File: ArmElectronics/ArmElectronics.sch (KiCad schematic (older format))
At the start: 66 parts, among them J1 Raspberry_Pi_2_3, J2 Power In, Q1 BSS138, Q10 BSS138, Q11 BSS138, Q12 BSS138, Q13 BSS138, Q14 BSS138, Q15 BSS138, Q16 BSS138, Q17 BSS138, Q18 BSS138, Q2 BSS138, Q3 BSS138, Q4 BSS138, Q5 BSS138, Q6 BSS138, Q7 BSS138, Q8 BSS138, Q9 BSS138, U1 Teensy4.1, U10 PA-09, U2 Pololu_2857, U3 Pololu_2851, U4 BNO055_Adafruit_Breakout, U5 TB9051FTG, U6 TB9051FTG, U7 TB9051FTG, U8 PA-09, U9 PA-09

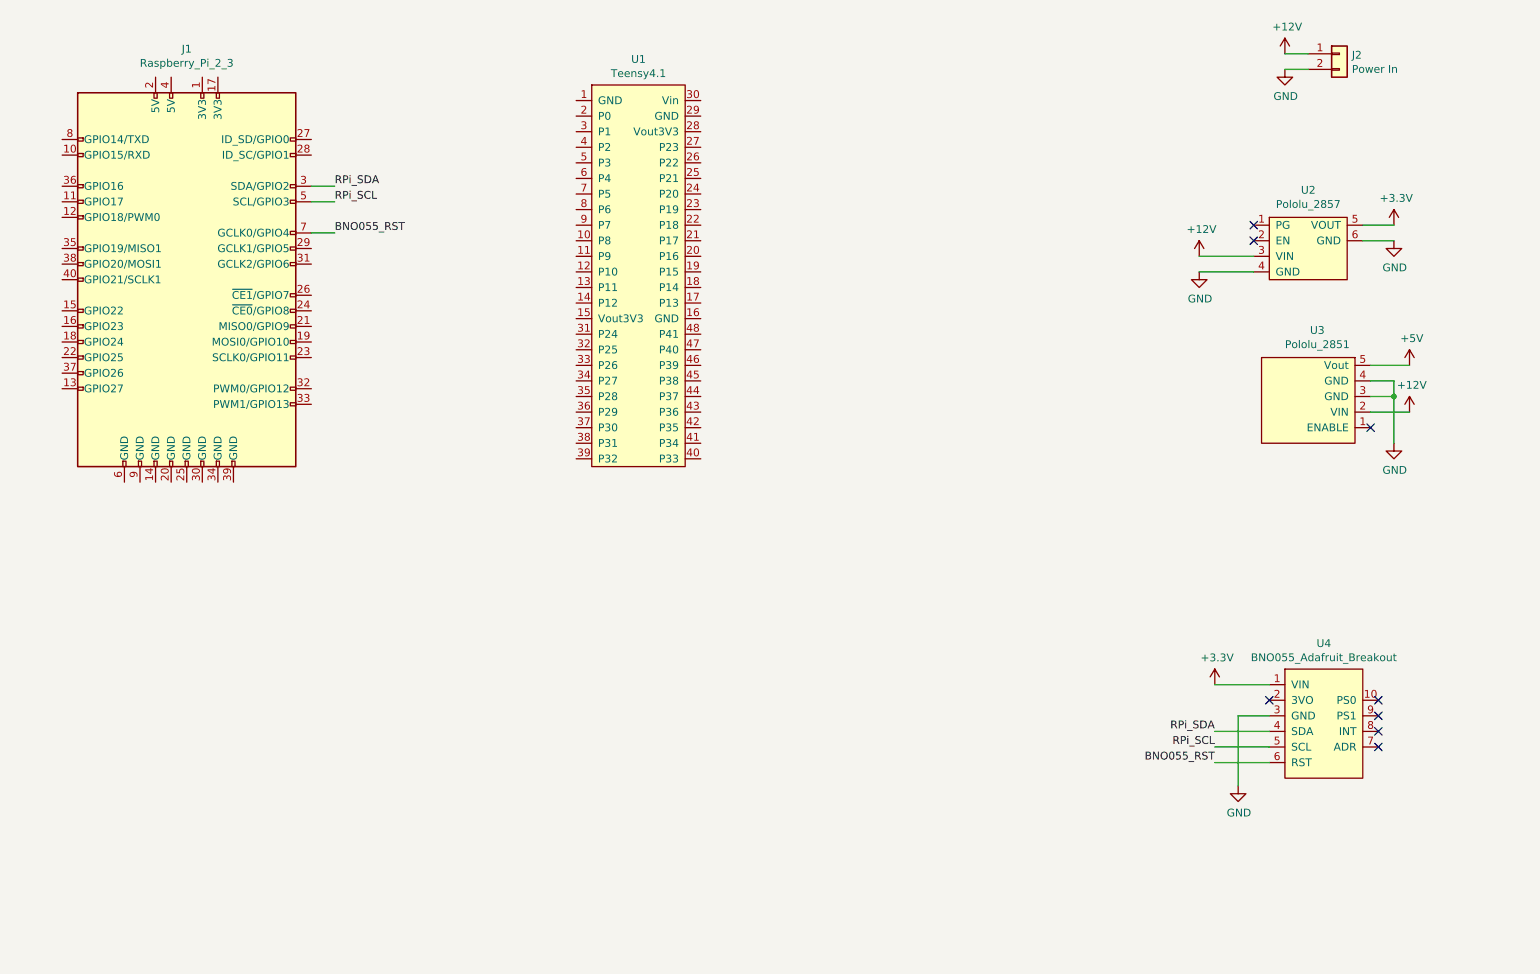
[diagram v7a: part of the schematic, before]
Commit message: connected rpi and teensy
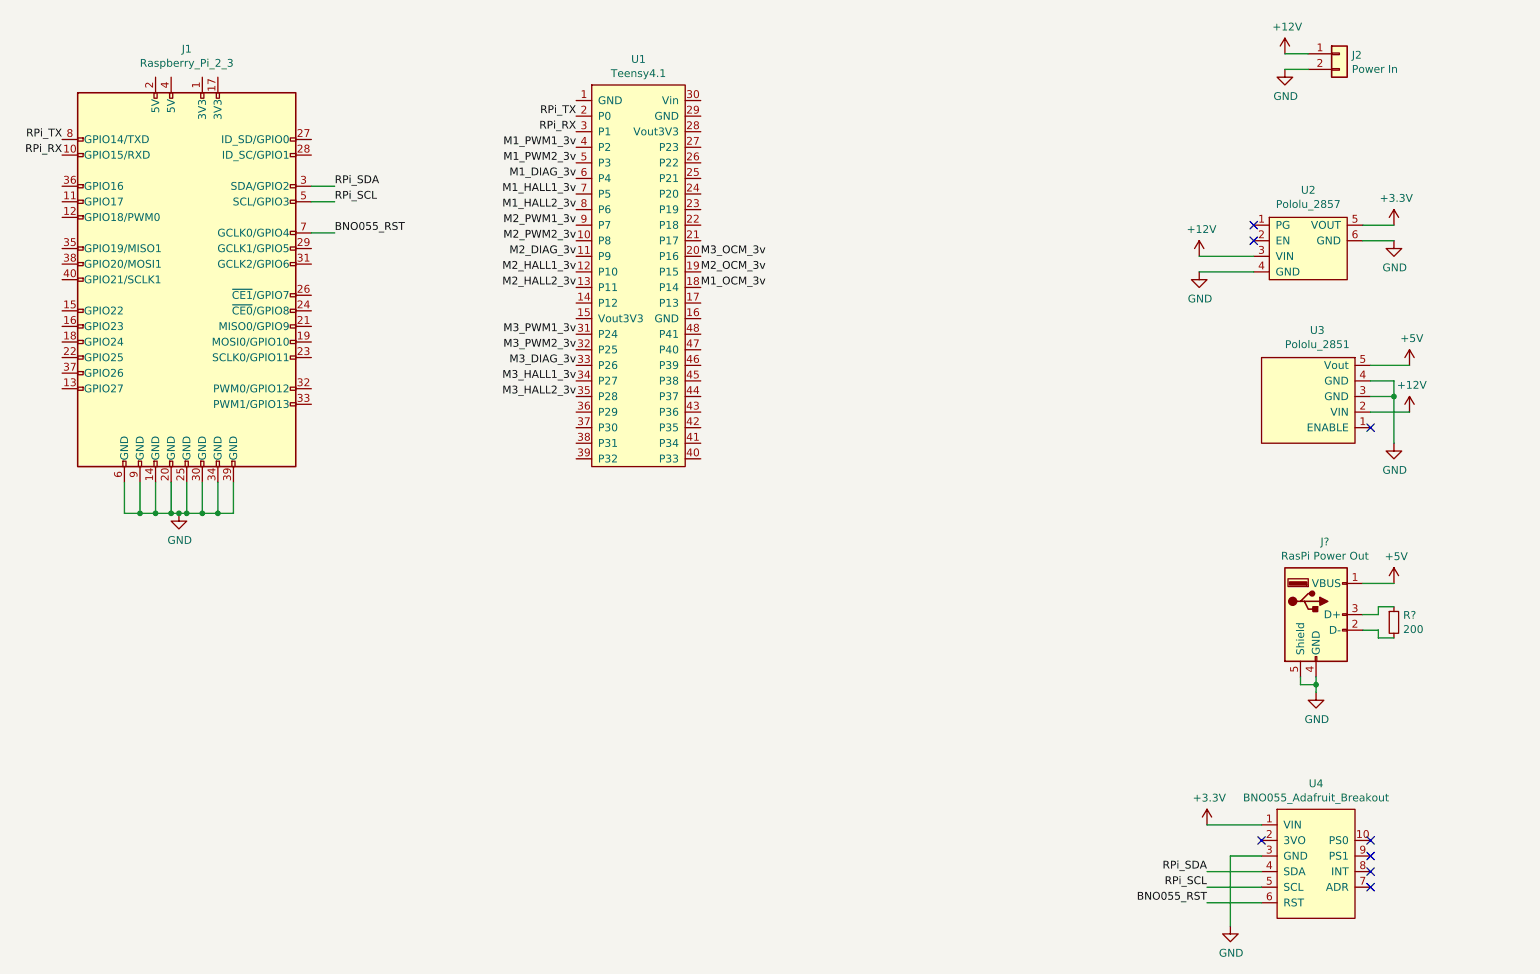
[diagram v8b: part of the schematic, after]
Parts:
- added J?: RasPi Power Out, symbol Connector:USB_A
- added R?: 200, symbol Device:R_Small
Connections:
- net +5V: now also J?.1 (VBUS)
- net GND: now also J1.14 (GND), J1.20 (GND), J1.25 (GND), J1.30 (GND), J1.34 (GND), J1.39 (GND), J1.6 (GND), J1.9 (GND), J?.4 (GND), J?.5 (Shield)
- net M1_DIAG_3v: now also U1.6 (P4)
- net M1_HALL1_3v: now also U1.7 (P5)
- net M1_HALL2_3v: now also U1.8 (P6)
- net M1_OCM_3v: now also U1.18 (P14)
- net M1_PWM1_3v: now also U1.4 (P2)
- net M1_PWM2_3v: now also U1.5 (P3)
- net M2_DIAG_3v: now also U1.11 (P9)
- net M2_HALL1_3v: now also U1.12 (P10)
- net M2_HALL2_3v: now also U1.13 (P11)
- net M2_OCM_3v: now also U1.19 (P15)
- net M2_PWM1_3v: now also U1.9 (P7)
- net M2_PWM2_3v: now also U1.10 (P8)
- net M3_DIAG_3v: now also U1.33 (P26)
- net M3_HALL1_3v: now also U1.34 (P27)
- net M3_HALL2_3v: now also U1.35 (P28)
- net M3_OCM_3v: now also U1.20 (P16)
- net M3_PWM1_3v: now also U1.31 (P24)
- net M3_PWM2_3v: now also U1.32 (P25)
- net RPi_RX: now reaches J1.10 (GPIO15/RXD)
- net RPi_RX: now also U1.3 (P1)
- net RPi_TX: now reaches J1.8 (GPIO14/TXD)
- net RPi_TX: now also U1.2 (P0)
- new net: J?.2 (D-), R?.2
- new net: J?.3 (D+), R?.1
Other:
- moved on the sheet: U4
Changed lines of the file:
@@
 L ArmElectronics_Library:BNO055_Adafruit_Breakout U4
 U 1 1 5F72BC87
-P 9400 5400
-F 0 "U4" H 9400 5915 50  0000 C CNN
-F 1 "BNO055_Adafruit_Breakout" H 9400 5824 50  0000 C CNN
-F 2 "" H 9400 5200 50  0001 C CNN
-F 3 "" H 9400 5200 50  0001 C CNN
-	1    9400 5400
+P 9350 6300
+F 0 "U4" H 9350 6815 50  0000 C CNN
+F 1 "BNO055_Adafruit_Breakout" H 9350 6724 50  0000 C CNN
+F 2 "" H 9350 6100 50  0001 C CNN
+F 3 "" H 9350 6100 50  0001 C CNN
+	1    9350 6300
 	1    0    0    -1
 $EndComp
@@
 L power:+3.3V #PWR?
 U 1 1 5F97F9E7
-P 8700 5150
-F 0 "#PWR?" H 8700 5000 50  0001 C CNN
-F 1 "+3.3V" H 8715 5323 50  0000 C CNN
-F 2 "" H 8700 5150 50  0001 C CNN
-F 3 "" H 8700 5150 50  0001 C CNN
-	1    8700 5150
-	1    0    0    -1
-$EndComp
-Wire Wire Line
-	8700 5150 9050 5150
-NoConn ~ 9050 5250
+P 8650 6050
+F 0 "#PWR?" H 8650 5900 50  0001 C CNN
+F 1 "+3.3V" H 8665 6223 50  0000 C CNN
+F 2 "" H 8650 6050 50  0001 C CNN
+F 3 "" H 8650 6050 50  0001 C CNN
+	1    8650 6050
+	1    0    0    -1
+$EndComp
+Wire Wire Line
+	8650 6050 9000 6050
+NoConn ~ 9000 6150
 $Comp
 L power:GND #PWR?
 U 1 1 5F9C4909
-P 8850 5800
-F 0 "#PWR?" H 8850 5550 50  0001 C CNN
-F 1 "GND" H 8855 5627 50  0000 C CNN
-F 2 "" H 8850 5800 50  0001 C CNN
-F 3 "" H 8850 5800 50  0001 C CNN
-	1    8850 5800
-	1    0    0    -1
-$EndComp
-Wire Wire Line
-	9050 5350 8850 5350
-Wire Wire Line
-	8850 5350 8850 5800
-Text Label 8700 5450 2    50   ~ 0
+P 8800 6700
+F 0 "#PWR?" H 8800 6450 50  0001 C CNN
+F 1 "GND" H 8805 6527 50  0000 C CNN
+F 2 "" H 8800 6700 50  0001 C CNN
+F 3 "" H 8800 6700 50  0001 C CNN
+	1    8800 6700
+	1    0    0    -1
+$EndComp
+Wire Wire Line
+	9000 6250 8800 6250
+Wire Wire Line
+	8800 6250 8800 6700
+Text Label 8650 6350 2    50   ~ 0
 RPi_SDA
-Text Label 8700 5550 2    50   ~ 0
+Text Label 8650 6450 2    50   ~ 0
 RPi_SCL
 Wire Wire Line
-	8700 5450 9050 5450
-Wire Wire Line
-	8700 5550 9050 5550
-NoConn ~ 9750 5250
-NoConn ~ 9750 5350
-NoConn ~ 9750 5450
-NoConn ~ 9750 5550
-Text Label 8700 5650 2    50   ~ 0
+	8650 6350 9000 6350
+Wire Wire Line
+	8650 6450 9000 6450
+NoConn ~ 9700 6150
+NoConn ~ 9700 6250
+NoConn ~ 9700 6350
+NoConn ~ 9700 6450
+Text Label 8650 6550 2    50   ~ 0
 BNO055_RST
 Wire Wire Line
-	8700 5650 9050 5650
+	8650 6550 9000 6550
 Text Label 3050 1950 0    50   ~ 0
 RPi_SDA
@@
 Wire Wire Line
 	3050 2250 2900 2250
+$Comp
+L Connector:USB_A J?
+U 1 1 5F8F258C
+P 9350 4700
+F 0 "J?" H 9407 5167 50  0000 C CNN
+F 1 "RasPi Power Out" H 9407 5076 50  0000 C CNN
+F 2 "" H 9500 4650 50  0001 C CNN
+F 3 " ~" H 9500 4650 50  0001 C CNN
+	1    9350 4700
+	1    0    0    -1
+$EndComp
+$Comp
+L Device:R_Small R?
+U 1 1 5F9045DB
+P 9850 4750
+F 0 "R?" H 9909 4796 50  0000 L CNN
+F 1 "200" H 9909 4705 50  0000 L CNN
+F 2 "" H 9850 4750 50  0001 C CNN
+F 3 "~" H 9850 4750 50  0001 C CNN
+	1    9850 4750
+	1    0    0    -1
+$EndComp
+Wire Wire Line
+	9650 4700 9750 4700
+Wire Wire Line
+	9750 4700 9750 4650
+Wire Wire Line
+	9750 4650 9850 4650
+Wire Wire Line
+	9850 4850 9750 4850
+Wire Wire Line
+	9750 4850 9750 4800
+Wire Wire Line
+	9750 4800 9650 4800
+$Comp
+L power:+5V #PWR?
+U 1 1 5F926B4C
+P 9850 4500
+F 0 "#PWR?" H 9850 4350 50  0001 C CNN
+F 1 "+5V" H 9865 4673 50  0000 C CNN
+F 2 "" H 9850 4500 50  0001 C CNN
+F 3 "" H 9850 4500 50  0001 C CNN
+	1    9850 4500
+	1    0    0    -1
+$EndComp
+Wire Wire Line
+	9850 4500 9650 4500
+$Comp
+L power:GND #PWR?
+U 1 1 5F93795A
+P 9350 5200
+F 0 "#PWR?" H 9350 4950 50  0001 C CNN
+F 1 "GND" H 9355 5027 50  0000 C CNN
+F 2 "" H 9350 5200 50  0001 C CNN
+F 3 "" H 9350 5200 50  0001 C CNN
+	1    9350 5200
+	1    0    0    -1
+$EndComp
+Wire Wire Line
+	9350 5200 9350 5150
+Wire Wire Line
+	9350 5150 9250 5150
+Wire Wire Line
+	9250 5150 9250 5100
+Wire Wire Line
+	9350 5100 9350 5150
+Connection ~ 9350 5150
+$Comp
+L power:GND #PWR?
+U 1 1 5F95A831
+P 2050 4050
+F 0 "#PWR?" H 2050 3800 50  0001 C CNN
+F 1 "GND" H 2055 3877 50  0000 C CNN
+F 2 "" H 2050 4050 50  0001 C CNN
+F 3 "" H 2050 4050 50  0001 C CNN
+	1    2050 4050
+	1    0    0    -1
+$EndComp
+Wire Wire Line
+	1700 3850 1700 4050
+Wire Wire Line
+	1700 4050 1800 4050
+Wire Wire Line
+	2050 4050 2100 4050
+Wire Wire Line
+	2400 4050 2400 3850
+Connection ~ 2050 4050
+Wire Wire Line
+	2300 3850 2300 4050
+Connection ~ 2300 4050
+Wire Wire Line
+	2300 4050 2400 4050
+Wire Wire Line
+	2200 3850 2200 4050
+Connection ~ 2200 4050
+Wire Wire Line
+	2200 4050 2300 4050
+Wire Wire Line
+	2100 3850 2100 4050
+Connection ~ 2100 4050
+Wire Wire Line
+	2100 4050 2200 4050
+Wire Wire Line
+	2000 3850 2000 4050
+Connection ~ 2000 4050
+Wire Wire Line
+	2000 4050 2050 4050
+Wire Wire Line
+	1900 3850 1900 4050
+Connection ~ 1900 4050
+Wire Wire Line
+	1900 4050 2000 4050
+Wire Wire Line
+	1800 3850 1800 4050
+Connection ~ 1800 4050
+Wire Wire Line
+	1800 4050 1900 4050
+Text Label 1300 1650 2    50   ~ 0
+RPi_TX
+Text Label 1300 1750 2    50   ~ 0
+RPi_RX
+Text Label 4600 1500 2    50   ~ 0
+RPi_TX
+Text Label 4600 1600 2    50   ~ 0
+RPi_RX
+Text Label 4600 1700 2    50   ~ 0
+M1_PWM1_3v
+Text Label 4600 1800 2    50   ~ 0
+M1_PWM2_3v
+Text Label 4600 2100 2    50   ~ 0
+M1_HALL2_3v
+Text Label 4600 2000 2    50   ~ 0
+M1_HALL1_3v
+Text Label 4600 1900 2    50   ~ 0
+M1_DIAG_3v
+Text Label 5400 2600 0    50   ~ 0
+M1_OCM_3v
+Text Label 4600 2200 2    50   ~ 0
+M2_PWM1_3v
+Text Label 4600 2300 2    50   ~ 0
+M2_PWM2_3v
+Text Label 4600 2600 2    50   ~ 0
+M2_HALL2_3v
+Text Label 4600 2500 2    50   ~ 0
+M2_HALL1_3v
+Text Label 4600 2400 2    50   ~ 0
+M2_DIAG_3v
+Text Label 4600 2900 2    50   ~ 0
+M3_PWM1_3v
+Text Label 4600 3000 2    50   ~ 0
+M3_PWM2_3v
+Text Label 4600 3300 2    50   ~ 0
+M3_HALL2_3v
+Text Label 4600 3200 2    50   ~ 0
+M3_HALL1_3v
+Text Label 4600 3100 2    50   ~ 0
+M3_DIAG_3v
+Text Label 5400 2500 0    50   ~ 0
+M2_OCM_3v
+Text Label 5400 2400 0    50   ~ 0
+M3_OCM_3v
 $EndSCHEMATC
